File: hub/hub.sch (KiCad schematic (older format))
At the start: 0 parts

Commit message: got all parts except usb a
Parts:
- added C1, C3, C5: 100nF, Capacitor_SMD:C_0603_1608Metric, symbol Device:C_Small
- added C2, C4, C6: 10uF, Capacitor_SMD:C_0805_2012Metric, symbol Device:CP_Small
- added D1: Power, LED_SMD:LED_0603_1608Metric, symbol Device:LED
- added D2: Port_1, LED_SMD:LED_0603_1608Metric, symbol Device:LED
- added D3: Port_3, LED_SMD:LED_0603_1608Metric, symbol Device:LED
- added D4: Port_2, LED_SMD:LED_0603_1608Metric, symbol Device:LED
- added D5: Port_4, LED_SMD:LED_0603_1608Metric, symbol Device:LED
- added D6: HUB_STATUS, LED_SMD:LED_0805_2012Metric_Castellated, symbol Device:LED
- added J1: C10418, usb_b_micro:C10418, symbol C10418:C10418
- added J2, J3, J4, J5: USB_A, symbol Connector:USB_A
- added R1, R3, R4: 1.5K, Resistor_SMD:R_0603_1608Metric, symbol Device:R_Small
- added R2: 2.7K, Resistor_SMD:R_0603_1608Metric, symbol Device:R_Small
- added U1: FE1.1s, Package_SO:SSOP-28_3.9x9.9mm_P0.635mm, symbol Interface_USB:FE1.1s
- added Y1: 12Mhz, symbol Device:Crystal_GND24_Small
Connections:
- new net: R2.2, U1.14 (REXT)
- new net: U1.2 (XOUT), Y1.3
- new net: U1.3 (XIN), Y1.1
- new net: D1.2 (A), R1.2
- new net: D2.2 (A), D3.1 (K), R3.2
- new net: D4.2 (A), D5.1 (K), R4.2
- new net +1V8: C5.1, C6.1, U1.12 (VD18_O), U1.28 (VD18)
- new net +3V3: C3.1, C4.1, U1.13 (VD33), U1.17 (~XRSTJ), U1.18 (VBUSM), U1.19 (BUSJ), U1.21 (VD33_O), U1.26 (OVCJ)
- new net +5V: C1.1, C2.1, J1.1, J2.1 (VBUS), J3.1 (VBUS), J4.1 (VBUS), J5.1 (VBUS), R1.1, U1.20 (VDD5)
- new net D1_N: J2.2 (D-), U1.10 (DM1)
- new net D1_P: J2.3 (D+), U1.11 (DP1)
- new net D2_N: J3.2 (D-), U1.8 (DM2)
- new net D2_P: J3.3 (D+), U1.9 (DP2)
- new net D3_N: J4.2 (D-), U1.6 (DM3)
- new net D3_P: J4.3 (D+), U1.7 (DP3)
- new net D4_N: J5.2 (D-), U1.4 (DM4)
- new net D4_P: J5.3 (D+), U1.5 (DP4)
- new net DRV: D2.1 (K), D3.2 (A), D4.1 (K), D5.2 (A), D6.2 (A), U1.22 (DRV)
- new net D_N: J1.2, U1.15 (DMU)
- new net D_P: J1.3, U1.16 (DPU)
- new net GND: C1.2, C2.2, C3.2, C4.2, C5.2, C6.2, D1.1 (K), D6.1 (K), J1.5, J1.6 (MH1), J1.7 (MH2), J1.8 (MH3), J1.9 (MH4), J2.4 (GND), J2.5 (Shield), J3.4 (GND), J3.5 (Shield), J4.4 (GND), J4.5 (Shield), J5.4 (GND), J5.5 (Shield), R2.1, U1.1 (VSS)
- new net LED_1: R3.1, U1.23 (LED1/EESCL)
- new net LED_2: R4.1, U1.24 (LED2)
- no-connect marks 0 -> 5

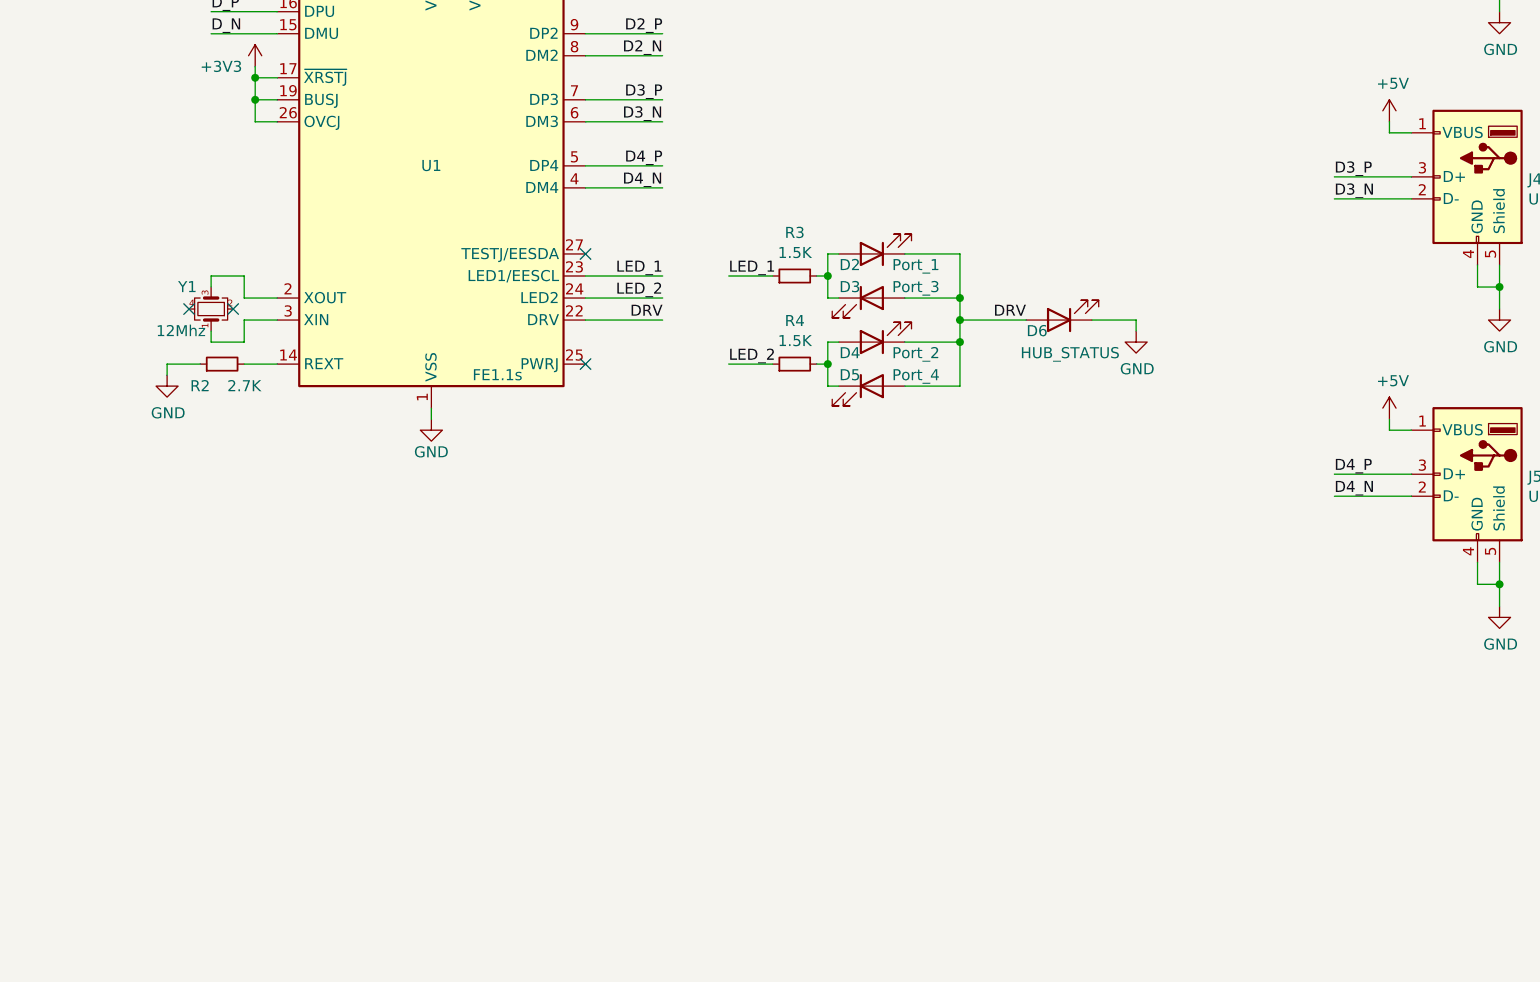
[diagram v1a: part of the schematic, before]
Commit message: V3.4 finished and ordered
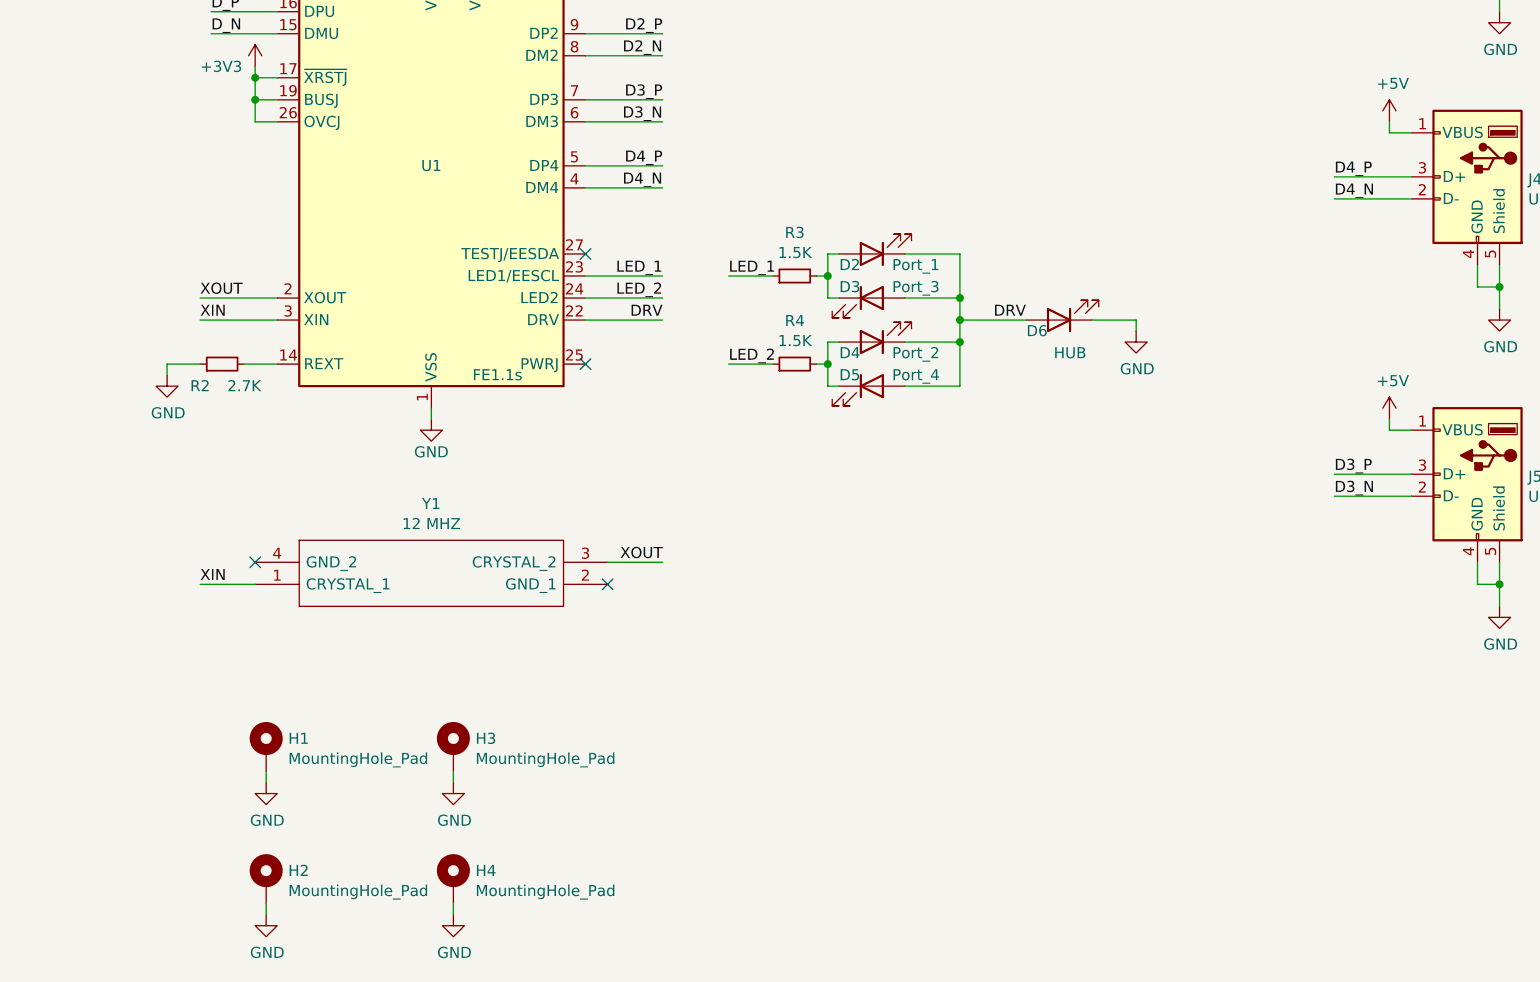
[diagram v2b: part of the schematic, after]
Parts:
- removed Y1: 12Mhz, symbol Device:Crystal_GND24_Small
- added H1, H2, H3, H4: MountingHole_Pad, MountingHole:MountingHole_2.7mm_M2.5_Pad_Via, symbol Mechanical:MountingHole_Pad
- added Y1: 12 MHZ, crystal_12MHz:X322512MSB4SI, symbol X322512MSB4SI:X322512MSB4SI
- C1, C3, C5: LCSC (none) -> C14663; LCSC Part # (none) -> C14663
- C2, C4, C6: LCSC (none) -> C15850; LCSC Part # (none) -> C15850
- D1: LCSC (none) -> C72043; LCSC Part # (none) -> C72043
- D2, D3, D4, D5: LCSC (none) -> C72041; LCSC Part # (none) -> C72041
- D6: value HUB_STATUS -> HUB; LCSC (none) -> C84256; LCSC Part # (none) -> C84256
- J1: Description USB Connectors SMD RoHS -> (none); LCSC (none) -> C10418; LCSC Part # (none) -> C10418
- J2, J3, J4, J5: footprint (none) -> SamacSys_Parts:676430910; LCSC (none) -> C42664; LCSC Part # (none) -> C42664
- R1, R3, R4: LCSC (none) -> C22843; LCSC Part # (none) -> C22843
- R2: LCSC (none) -> C13167; LCSC Part # (none) -> C13167
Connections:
- net D3_N: now also J5.2 (D-); no longer J4.2 (D-)
- net D3_P: now also J5.3 (D+); no longer J4.3 (D+)
- net D4_N: now also J4.2 (D-); no longer J5.2 (D-)
- net D4_P: now also J4.3 (D+); no longer J5.3 (D+)
- net GND: now also H1.1, H2.1, H3.1, H4.1
- net XOUT: now reaches U1.2 (XOUT)
- net XOUT: now also Y1.3 (CRYSTAL_2)
- net XIN: now reaches U1.3 (XIN)
- net XIN: now also Y1.1 (CRYSTAL_1)
